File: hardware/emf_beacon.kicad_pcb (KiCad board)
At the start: 2 copper layers, 100 x 100 mm, 119 parts, among them J1 USB_C_Receptacle_USB2.0_16P, J10 Conn_01x02, J11 Conn_01x02, J12 Conn_01x02, J13 Conn_01x02, J14 Conn_01x02, J2 Conn_01x06, J3 Conn_01x06, J4 Conn_01x02, J5 Conn_01x02, J6 Conn_01x02, J7 Conn_01x02, J8 Conn_01x02, J9 Conn_01x02, Q1 AO3400A, Q10 AO3400A, Q11 DMP3013SFV, Q12 AO3400A, Q2 AO3400A, Q3 AO3400A, Q4 AO3400A, Q5 AO3400A, Q6 AO3400A, Q7 AO3400A, Q8 AO3400A, Q9 AO3400A, SW1 SW_DIP_x10, SW2 SW_Push, U1 ESP32-C3-WROOM-02, U2 MCP23017T-E/SS, U3 CA-IS3092W, U4 PCA9685PW, U5 ZTP7193MA, U6 FP6151XR-G1

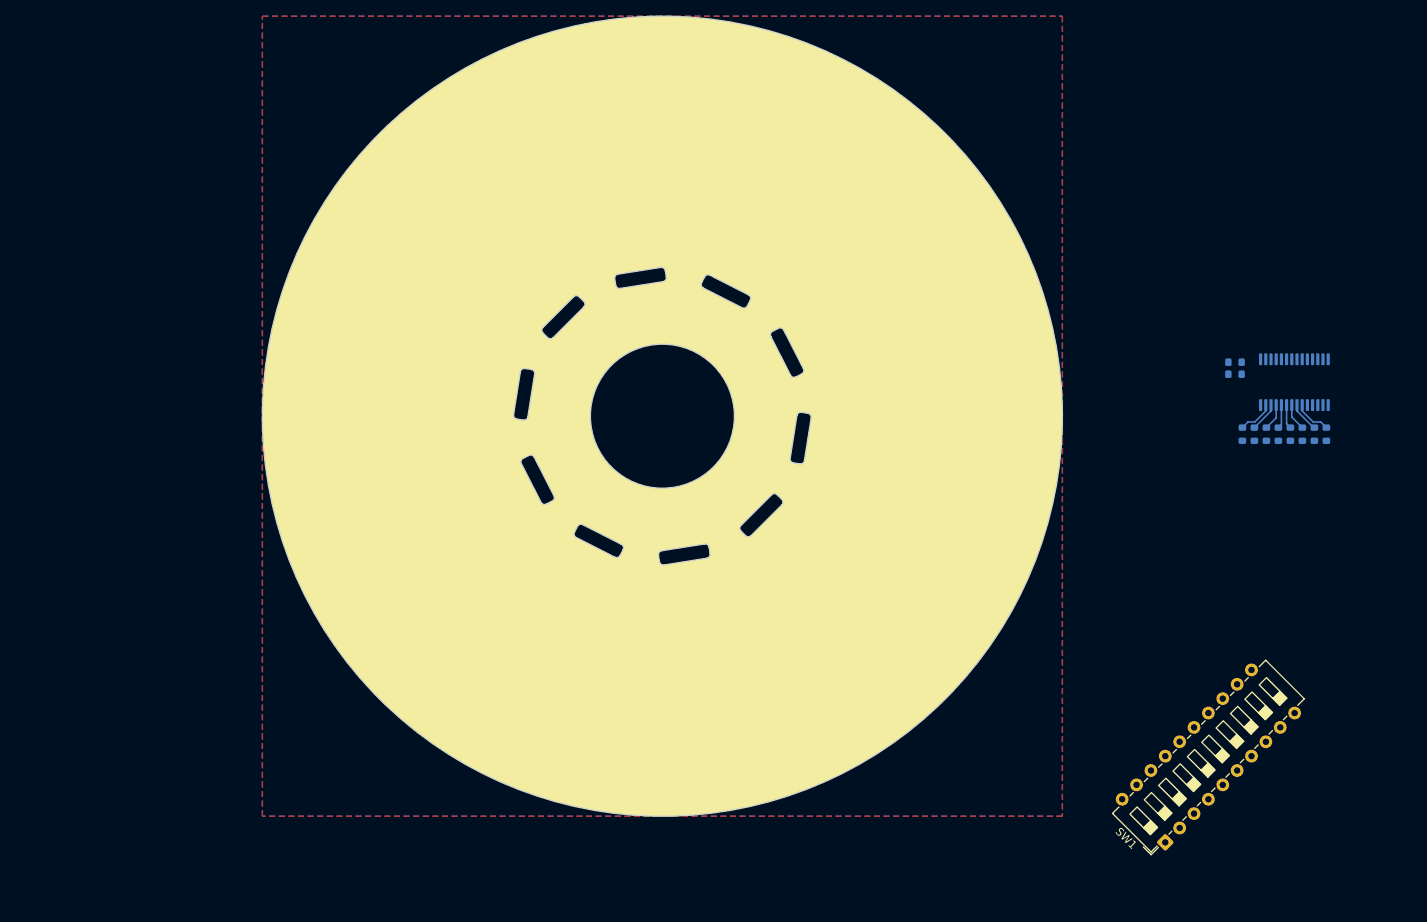
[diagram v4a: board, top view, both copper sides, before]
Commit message: adding snubbers, starting placement
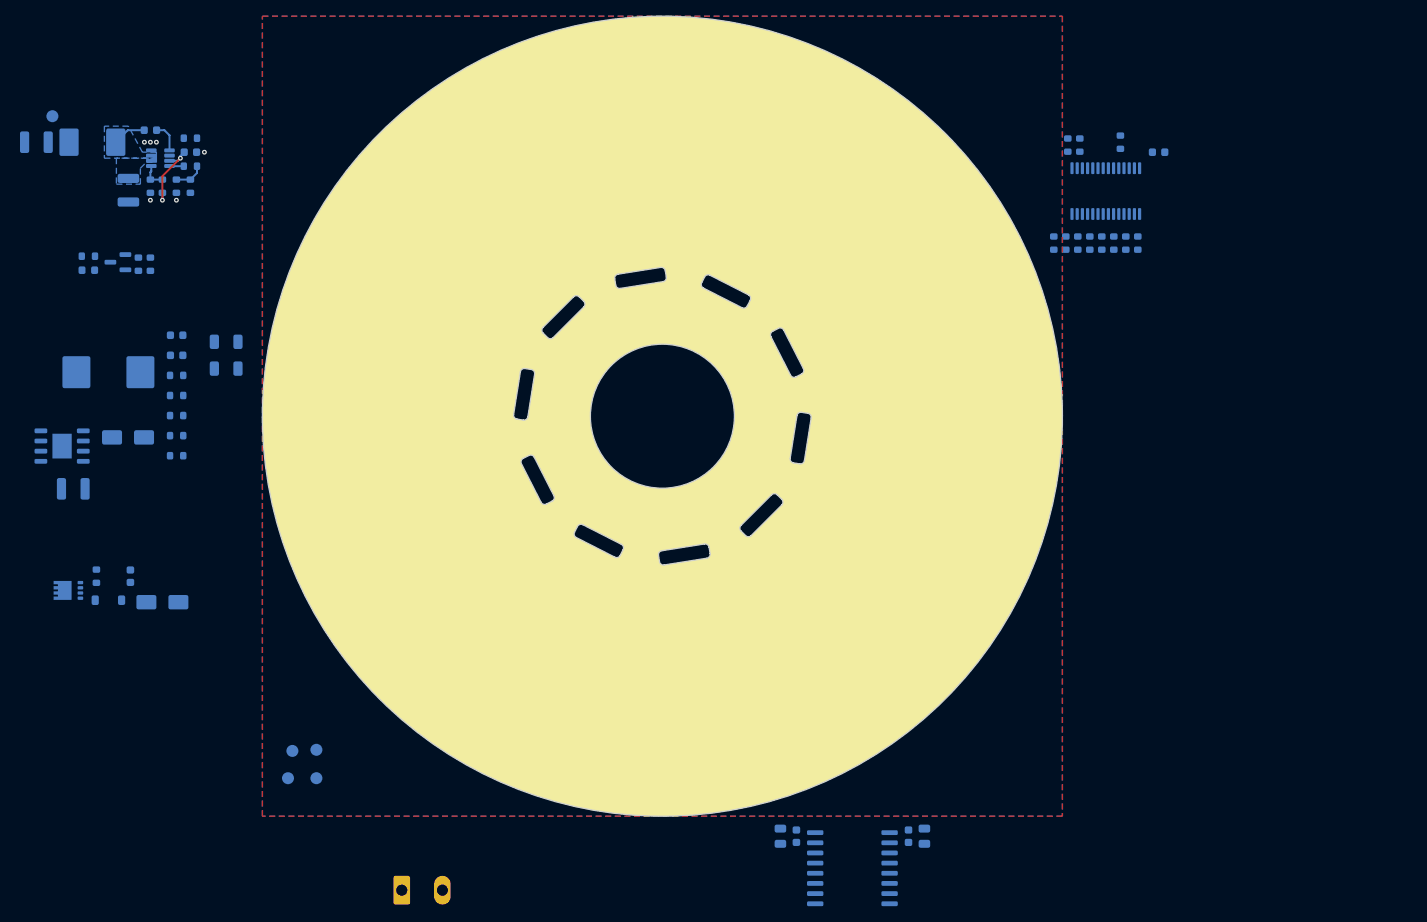
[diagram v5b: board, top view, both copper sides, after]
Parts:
- added C28: 10nF, Capacitor_SMD:C_0603_1608Metric, B.Cu at (165.5, 119.0)
- added C29: 10nF, Capacitor_SMD:C_0603_1608Metric, B.Cu at (151.8, 122.8)
- added C30: 10nF, Capacitor_SMD:C_0603_1608Metric, B.Cu at (136.2, 119.5)
- added C31: 10nF, Capacitor_SMD:C_0603_1608Metric, B.Cu at (127.5, 107.5)
- added C32: 10nF, Capacitor_SMD:C_0603_1608Metric, B.Cu at (125.5, 93.8)
- added C33: 10nF, Capacitor_SMD:C_0603_1608Metric, B.Cu at (134.5, 80.8)
- added C34: 10nF, Capacitor_SMD:C_0603_1608Metric, B.Cu at (147.2, 75.5)
- added C35: 10nF, Capacitor_SMD:C_0603_1608Metric, B.Cu at (162.0, 79.2)
- added C36: 10nF, Capacitor_SMD:C_0603_1608Metric, B.Cu at (172.0, 90.2)
- added C37: 10nF, Capacitor_SMD:C_0603_1608Metric, B.Cu at (173.0, 105.2)
- added R44: 10R, Resistor_SMD:R_0603_1608Metric, B.Cu at (151.8, 124.2)
- added R45: 10R, Resistor_SMD:R_0603_1608Metric, B.Cu at (136.2, 121.0)
- added R46: 10R, Resistor_SMD:R_0603_1608Metric, B.Cu at (127.5, 109.0)
- added R47: 10R, Resistor_SMD:R_0603_1608Metric, B.Cu at (125.5, 95.2)
- added R48: 10R, Resistor_SMD:R_0603_1608Metric, B.Cu at (134.5, 82.5)
- added R49: 10R, Resistor_SMD:R_0603_1608Metric, B.Cu at (147.2, 77.0)
- added R50: 10R, Resistor_SMD:R_0603_1608Metric, B.Cu at (162.0, 80.8)
- added R51: 10R, Resistor_SMD:R_0603_1608Metric, B.Cu at (172.0, 91.8)
- added R52: 10R, Resistor_SMD:R_0603_1608Metric, B.Cu at (173.0, 106.8)
- R9: value 120R -> 10R; footprint Resistor_SMD:R_0805_2012Metric -> Resistor_SMD:R_0603_1608Metric
- moved TP1 77.0 mm to (106.8, 141.7)
- moved TP2 77.0 mm to (103.8, 141.8)
- moved TP4 77.0 mm to (106.8, 145.2)
- moved TP3 77.0 mm to (103.2, 145.2)
- moved R12 76.8 mm to (162.0, 61.5)
- moved C3 70.0 mm to (121.8, 103.5)
- moved R3 70.0 mm to (121.8, 100.2)
- moved TH1 70.0 mm to (120.0, 103.5)
- moved C6 60.0 mm to (190.2, 98.8), turned to 90 degrees
- moved C11 59.2 mm to (212.0, 67.0)
- moved C16 56.9 mm to (83.2, 71.8)
- moved C17 56.9 mm to (91.0, 67.0)
- moved C21 56.9 mm to (86.0, 64.2)
- moved C23 56.9 mm to (71.8, 65.8)
- moved L2 56.9 mm to (78.8, 65.8)
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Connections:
- R9 pad 1: Net-(R9-Pad1) -> Net-(J4-Pin_2)
- R9 pad 2: /DMX512/DMX_DATA+ -> Net-(C28-Pad2)
- SW1 pad 10: Net-(R9-Pad1) -> GND
- SW1 pad 11: /DMX512/DMX_DATA- -> /CTRL/WIFI_~{ENABLE}
- U1 pad 4: unconnected-(U1-IO5-Pad4) -> /CTRL/WIFI_~{ENABLE}
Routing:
- net /CTRL/I2C_SDA: track 0.00 -> 38.2 mm
- net /CTRL/I2C_SCL: track 0.00 -> 36.4 mm
- net /DMX512/DMX_ADDR0: track 0.00 -> 18.2 mm, vias 0 -> 1
- net /CTRL/ESP_~{RST}: track 0.00 -> 16.8 mm, vias 0 -> 2
- net /DMX512/DMX_ADDR1: track 0.00 -> 16.5 mm, vias 0 -> 1
- net +3V3: track 0.00 -> 16.0 mm, vias 0 -> 4
- net /DMX512/DMX_ADDR2: track 0.00 -> 14.8 mm, vias 0 -> 1
- net /DMX512/DMX_ADDR3: track 0.00 -> 13.0 mm, vias 0 -> 1
- net /DMX512/DMX_ADDR4: track 0.00 -> 12.1 mm, vias 0 -> 1
- net /DMX512/DMX_ADDR5: track 0.00 -> 11.6 mm, vias 0 -> 1
- net /DMX512/DMX_ADDR6: track 0.00 -> 11.1 mm, vias 0 -> 1
- net /DMX512/DMX_DATA-: track 0.00 -> 9.00 mm
- net /DMX512/DMX_DATA+: track 0.00 -> 9.00 mm
- net GND_ISO: track 0.00 -> 9.00 mm
- net /DMX512/DMX_AUX+: track 0.00 -> 9.00 mm
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
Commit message: updating PSUs
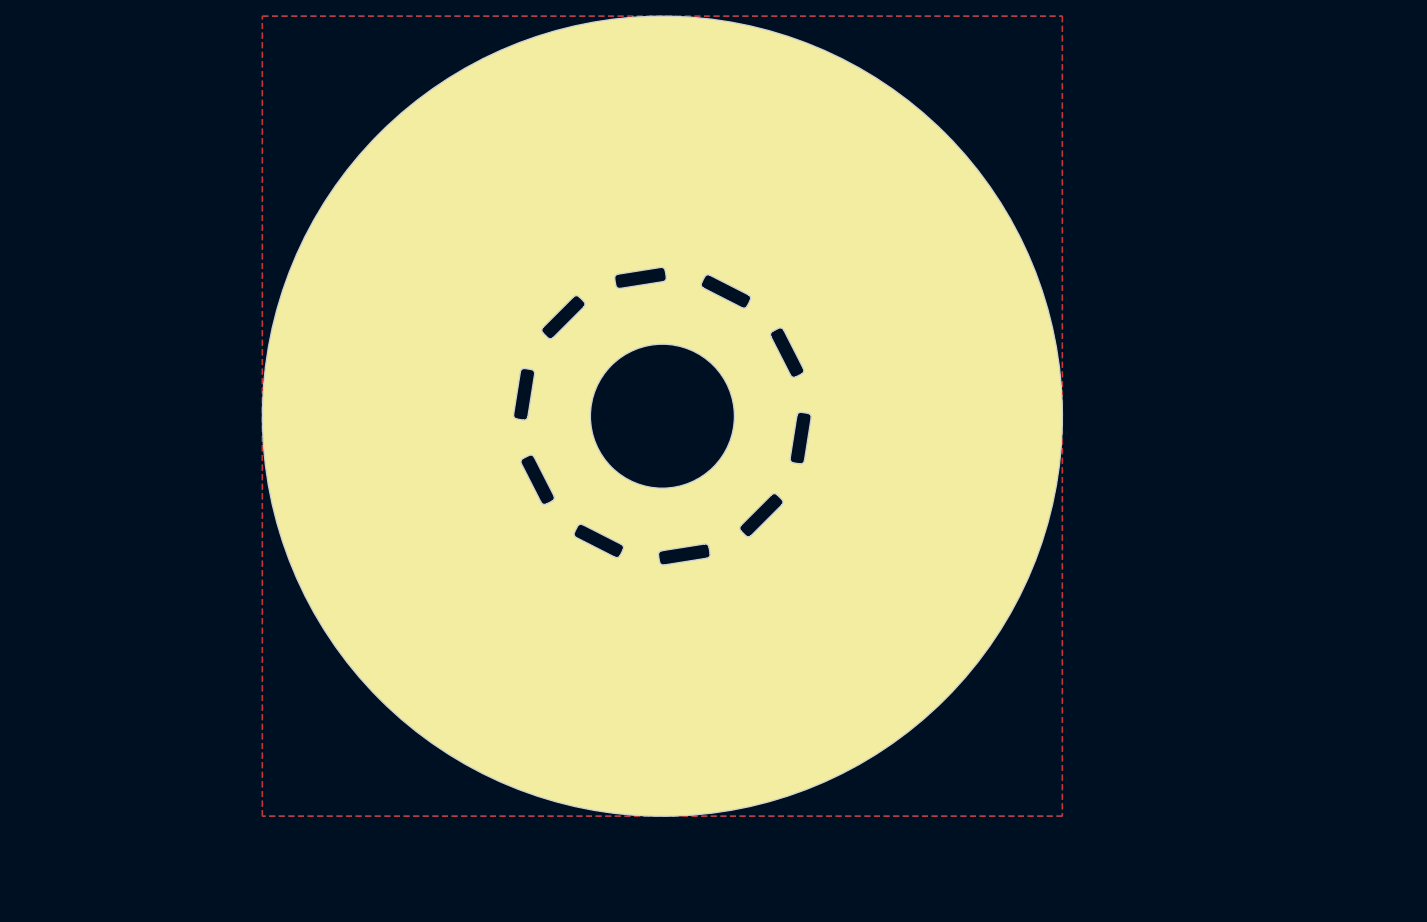
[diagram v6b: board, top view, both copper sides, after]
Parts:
- removed C16, C23: 47uF, Capacitor_SMD:C_1210_3225Metric
- removed C20, C21: 1uF, Capacitor_SMD:C_0603_1608Metric
- removed C22, C24: 22uF, Capacitor_SMD:C_1206_3216Metric
- removed D4: SS34, Diode_SMD:D_SMA
- removed L2: IHLP2525CZER100M01, Inductor_SMD:L_Vishay_IHLP-2525
- removed Q12: AO3400A, Package_TO_SOT_SMD:SOT-23
- removed R34: 150k, Resistor_SMD:R_0603_1608Metric
- removed R35: 16k, Resistor_SMD:R_0603_1608Metric
- removed R36: 43k, Resistor_SMD:R_0603_1608Metric
- removed R37: 8k2, Resistor_SMD:R_0603_1608Metric
- removed R38: 100R, Resistor_SMD:R_0603_1608Metric
- removed R39: 10k, Resistor_SMD:R_0603_1608Metric
- removed TP5: TestPoint, TestPoint:TestPoint_Pad_D1.5mm
- removed U6: FP6151XR-G1, Package_SO:HSOP-8-1EP_3.9x4.9mm_P1.27mm_EP2.41x3.1mm
- added C12: 100nF, Capacitor_SMD:C_0603_1608Metric, B.Cu at (106.2, 98.2)
- added C13: 10uF 25V, Capacitor_SMD:C_0805_2012Metric, B.Cu at (111.8, 98.2)
- added C38: 22uF 50V, Capacitor_SMD:C_1210_3225Metric, B.Cu at (117.1, 114.8)
- added C39: 1nF, Capacitor_SMD:C_0402_1005Metric, B.Cu at (110.4, 111.0)
- added C40: 22uF 10V, Capacitor_SMD:C_0805_2012Metric, B.Cu at (113.2, 116.8)
- added D6: 1N4148, Diode_SMD:D_SOD-123, B.Cu at (166.5, 64.5)
- added Q13: AO3400A, Package_TO_SOT_SMD:SOT-23, B.Cu at (118.8, 84.0)
- added R54: 430k, Resistor_SMD:R_0603_1608Metric, B.Cu at (105.9, 111.3)
- added R55: 82k, Resistor_SMD:R_0603_1608Metric, B.Cu at (105.9, 114.3)
- added TP6: TestPoint, TestPoint:TestPoint_Pad_D1.5mm, B.Cu at (173.8, 61.2)
- added U7: TPS82130SILR, Package_LGA:Texas_SIL0008D_MicroSiP-8-1EP_2.8x3mm_P0.65mm_EP1.1x1.9mm, B.Cu at (111.6, 113.5)
- C17: value 100nF -> 10uF 25V; footprint Capacitor_SMD:C_0603_1608Metric -> Capacitor_SMD:C_0805_2012Metric
- C18: value C -> 22uF 10V; footprint Capacitor_SMD:C_1210_3225Metric -> Capacitor_SMD:C_0805_2012Metric
- C19: value 470pF -> 10uF 25V; footprint Capacitor_SMD:C_0603_1608Metric -> Capacitor_SMD:C_0805_2012Metric
- C5: footprint Capacitor_SMD:C_1808_4520Metric -> Capacitor_SMD:C_1206_3216Metric
- L1: value JSHC1040H-4R7M-G -> MDE0840-3R3M; footprint Inductor_SMD:L_Wuerth_HCI-1040 -> Inductor_SMD:L_Vishay_IHLP-3232
- R27: value 33k -> R
- R28: value 91k -> R
- R29: value 10k -> 75k
- R30: value 100k -> 10k
- R31: value 10k -> 100R
- R32: value 200k -> 10k
- R33: value 33k -> 10k
- TH1: value NCP15XH103F03RC -> NCP18XH103F03RB
- U5: value ZTP7193MA -> TPS565208; footprint Package_TO_SOT_SMD:SOT-23-8 -> Package_TO_SOT_SMD:SOT-23-6
- moved TP2 102.6 mm to (171.5, 64.8)
- moved TP4 83.2 mm to (187.8, 126.2)
- moved LED1 62.8 mm to (136.7, 59.0)
- moved R40 61.4 mm to (136.8, 61.5)
- moved C14 48.6 mm to (132.1, 121.2)
- moved D2 48.6 mm to (129.3, 124.2)
- moved D3 48.6 mm to (136.1, 124.5)
- moved Q11 48.6 mm to (124.3, 123.0)
- moved R26 48.6 mm to (127.8, 121.2)
- moved R30 41.5 mm to (110.2, 102.0), turned to -90 degrees
- moved C18 40.2 mm to (107.8, 84.0), turned to 90 degrees
- moved R29 40.1 mm to (111.8, 102.0), turned to 90 degrees
- moved C17 38.7 mm to (113.8, 98.2), turned to -90 degrees
- moved U5 37.5 mm to (109.0, 98.2), turned to -90 degrees
- moved R28 37.4 mm to (108.8, 102.0), turned to -90 degrees
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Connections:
- C17 pad 1: GND -> VDC
- C17 pad 2: /POWER/VCC_3V3 -> GND
- C18 pad 1: unconnected-(C18-Pad1) -> +6V5
- C18 pad 2: unconnected-(C18-Pad2) -> GND
- C19 pad 1: Net-(U6-COMP) -> +6V5
- C19 pad 2: Net-(C19-Pad2) -> GND
- L1 pad 1: Net-(D4-K) -> Net-(U5-SW)
- LED1 pad 1: Net-(LED1-K) -> GND
- R27 pad 1: Net-(C19-Pad2) -> VDC
- R27 pad 2: GND -> Net-(U5-EN)
- R28 pad 1: /POWER/VCC_3V3 -> Net-(U5-EN)
- R28 pad 2: Net-(U5-AAM) -> GND
- R29 pad 1: Net-(U5-AAM) -> +6V5
- R29 pad 2: GND -> Net-(U5-VFB)
- R30 pad 1: VDC -> Net-(U5-VFB)
- R30 pad 2: Net-(U5-EN/SYNC) -> GND
- R31 pad 1: VDC -> +6V5
- R31 pad 2: Net-(U6-EN) -> Net-(Q13-G)
- R32 pad 1: Net-(U6-RT) -> Net-(Q13-G)
- R33 pad 1: /POWER/FB_3V3 -> +3V3
- R33 pad 2: Net-(R33-Pad2) -> /POWER/LED_~{PGD}
- R40 pad 1: +6V5 -> unconnected-(R40-Pad1)
- U5 pad 1: Net-(U5-AAM) -> GND
- U5 pad 2: VDC -> Net-(U5-SW)
- U5 pad 3: /POWER/SW_3V3 -> VDC
- U5 pad 4: GND -> Net-(U5-VFB)
- U5 pad 5: Net-(U5-BOOT) -> Net-(U5-EN)
- U5 pad 6: Net-(U5-EN/SYNC) -> Net-(U5-VBST)
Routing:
- net /POWER/VCC_3V3: track 9.73 -> 0.00 mm, vias 2 -> 0
- net /CTRL/ESP_~{BOOT}: track 0.00 -> 8.56 mm
- net /POWER/SW_3V3: track 4.18 -> 0.00 mm
- net Net-(R33-Pad2): track 3.77 -> 0.00 mm
- net Net-(U5-BOOT): track 3.76 -> 0.00 mm
- net /CTRL/ESP_~{RST}: track 16.8 -> 20.2 mm
- net Net-(U5-AAM): track 3.25 -> 0.00 mm
- net /POWER/FB_3V3: track 1.80 -> 0.00 mm
- net GND: vias 7 -> 1
- removed copper zone on B.Cu, net /POWER/SW_3V3
- removed copper zone on B.Cu, net VDC

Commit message: some jlc cleanup
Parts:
- removed R27, R28: R, Resistor_SMD:R_0603_1608Metric
- added C15: 100uF 25V, Capacitor_SMD:CP_Elec_6.3x7.7, B.Cu at (120.0, 92.0)
- added C16: 100uF 16V, Capacitor_SMD:CP_Elec_6.3x7.7, B.Cu at (175.0, 113.0)
- C19: value 10uF 25V -> 22uF 10V
- C39: footprint Capacitor_SMD:C_0402_1005Metric -> Capacitor_SMD:C_0603_1608Metric
- D6: value 1N4148 -> BAT54WS; footprint Diode_SMD:D_SOD-123 -> Diode_SMD:D_SOD-323
- R54: value 430k -> 75k
- R55: value 82k -> 24k
- moved C18 0.50 mm to (107.2, 84.0)
- moved C19 0.25 mm to (110.8, 84.0)
- renumbered Q13 to Q11, Q11 to Q12
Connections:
- U5 pad 5: Net-(U5-EN) -> VDC
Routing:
- net +6V5: track 0.00 -> 22.2 mm, vias 0 -> 2
- net Net-(U5-VFB): track 0.00 -> 3.41 mm
- net VDC: track 0.00 -> 2.67 mm
- added copper zone on B.Cu, net +6V5
- added copper zone on B.Cu, net Net-(U5-SW)

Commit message: tweaking lcsc part numbers
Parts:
- removed C38: 22uF 50V, Capacitor_SMD:C_1210_3225Metric
- added C20: 10uF 25V, Capacitor_SMD:C_0805_2012Metric, B.Cu at (114.8, 113.2)
- added C21: 10uF 25V, Capacitor_SMD:C_0805_2012Metric, B.Cu at (116.8, 113.2)
- added C22: 10uF 25V, Capacitor_SMD:C_0805_2012Metric, B.Cu at (118.8, 113.2)
- C1, C10, C27, C7: value 10uF -> 10uF 25V
- C16: footprint Capacitor_SMD:CP_Elec_6.3x7.7 -> Capacitor_SMD:CP_Elec_6.3x5.7
- C3: value 1uF -> 1uF 50V
- U7: value TPS82130SILR -> TPS82140SILR
- moved R18 58.0 mm to (131.5, 115.0)
- moved R19 55.9 mm to (127.0, 101.8)
- moved R17 52.4 mm to (146.2, 123.8)
- moved R20 48.8 mm to (130.8, 88.0)
- moved R21 45.6 mm to (132.5, 84.2), turned to -45 degrees
- moved R16 42.2 mm to (157.2, 118.7)
- moved R25 37.8 mm to (169.5, 111.9)
- moved R22 33.3 mm to (145.0, 76.5), turned to -81 degrees
- moved R24 23.9 mm to (172.0, 98.5)
- moved R23 17.7 mm to (159.8, 78.5), turned to -117 degrees
- moved Q6 5.21 mm to (134.5, 82.5), turned to -45 degrees
- moved Q7 5.19 mm to (147.7, 76.8), turned to -81 degrees
- moved Q8 4.98 mm to (162.0, 80.0), turned to -117 degrees
- moved R49 4.03 mm to (150.8, 79.0), turned to 99 degrees
- moved R48 4.01 mm to (138.5, 82.8), turned to 135 degrees
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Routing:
- net +6V5: track 22.2 -> 34.9 mm
